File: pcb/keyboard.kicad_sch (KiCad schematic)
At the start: 60 parts, among them J1 Tag-Connect TC2030, J1 USB4510-03-1-A, J4 Battery, Q2 2N7002, SW1 PWR, U1 SRV05-4, U3 BQ24075, U3 BT840, Y1 32.768KHz

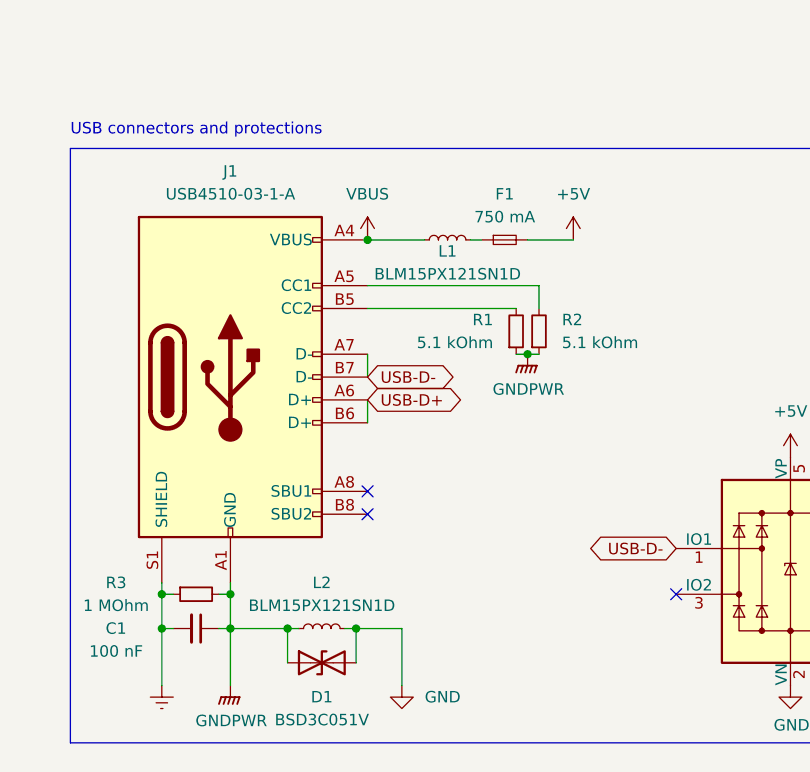
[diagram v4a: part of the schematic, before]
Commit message: #1 Change USB connector components to Digikey 0603
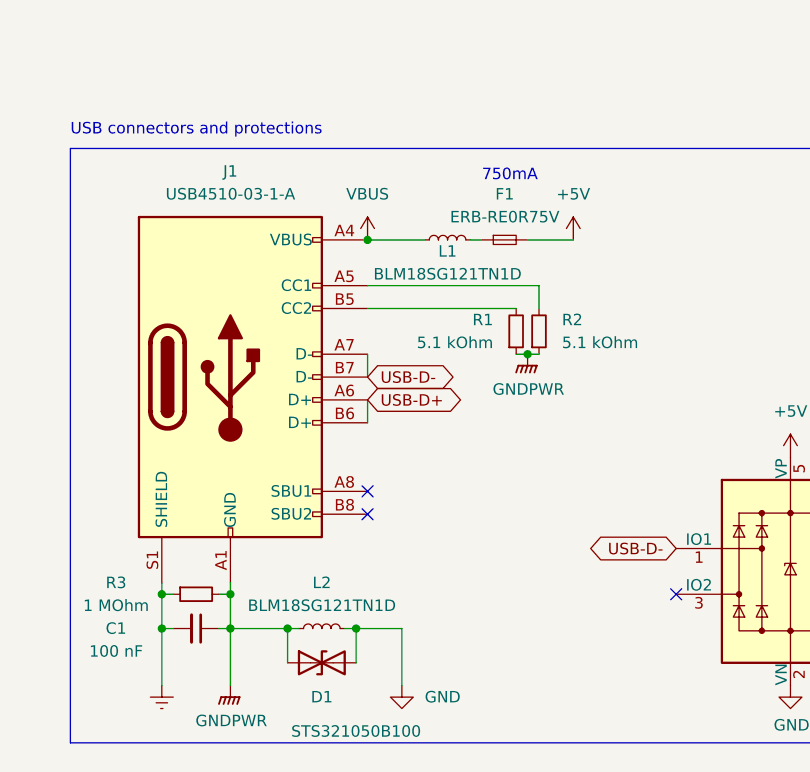
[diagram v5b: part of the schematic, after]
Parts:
- C1: footprint Capacitor_SMD:C_0402_1005Metric -> Capacitor_SMD:C_0603_1608Metric
- D1: value BSD3C051V -> STS321050B100
- F1: value 750 mA -> ERB-RE0R75V
- J1: footprint Connector_USB:USB_C_Receptacle_HRO_TYPE-C-31-M-12 -> keyboard:USB_C_Receptacle_GCT_USB4510-03-1-A
- L1, L2: value BLM15PX121SN1D -> BLM18SG121TN1D; footprint Inductor_SMD:L_0402_1005Metric -> Inductor_SMD:L_0603_1608Metric
- R1, R2, R3: footprint Resistor_SMD:R_0402_1005Metric -> Resistor_SMD:R_0603_1608Metric
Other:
- note added: "750mA"
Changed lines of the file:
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@@
     (effects (font (size 1.27 1.27)) (justify left bottom))
   )
+  (text "750mA" (at 67.31 213.36 0)
+    (effects (font (size 1.27 1.27)) (justify left bottom))
+  )
   (text "Battery management (advanced)" (at 242.57 26.67 0)
     (effects (font (size 1.27 1.27)) (justify left bottom))
@@
       (effects (font (size 1.27 1.27)) (justify right))
     )
-    (property "Footprint" "Resistor_SMD:R_0402_1005Metric" (at 71.12 229.87 0)
+    (property "Footprint" "Resistor_SMD:R_0603_1608Metric" (at 71.12 229.87 0)
       (effects (font (size 1.27 1.27)) hide)
     )
@@
       (effects (font (size 1.27 1.27)))
     )
-    (property "Value" "BLM15PX121SN1D" (at 63.5 223.52 90)
+    (property "Value" "BLM18SG121TN1D" (at 63.5 223.52 90)
       (effects (font (size 1.27 1.27)))
     )
-    (property "Footprint" "Inductor_SMD:L_0402_1005Metric" (at 63.5 219.71 0)
+    (property "Footprint" "Inductor_SMD:L_0603_1608Metric" (at 63.5 219.71 0)
       (effects (font (size 1.27 1.27)) hide)
     )
-    (property "Datasheet" "https://www.murata.com/en-us/products/productdata/8796740059166/ENFA0018.pdf" (at 63.5 219.71 0)
+    (property "Datasheet" "https://www.murata.com/en-us/products/productdata/8796738650142/ENFA0003.pdf" (at 63.5 219.71 0)
       (effects (font (size 1.27 1.27)) hide)
     )
@@
       (effects (font (size 1.27 1.27)))
     )
-    (property "Footprint" "Resistor_SMD:R_0402_1005Metric" (at 35.56 259.08 0)
+    (property "Footprint" "Resistor_SMD:R_0603_1608Metric" (at 35.56 259.08 0)
       (effects (font (size 1.27 1.27)) hide)
     )
@@
       (effects (font (size 1.27 1.27)))
     )
-    (property "Footprint" "Capacitor_SMD:C_0402_1005Metric" (at 35.56 262.89 0)
+    (property "Footprint" "Capacitor_SMD:C_0603_1608Metric" (at 35.56 262.89 0)
       (effects (font (size 1.27 1.27)) hide)
     )
@@
       (effects (font (size 1.27 1.27)))
     )
-    (property "Value" "BLM15PX121SN1D" (at 49.53 260.35 90)
+    (property "Value" "BLM18SG121TN1D" (at 49.53 260.35 90)
       (effects (font (size 1.27 1.27)))
     )
-    (property "Footprint" "Inductor_SMD:L_0402_1005Metric" (at 49.53 262.89 0)
+    (property "Footprint" "Inductor_SMD:L_0603_1608Metric" (at 49.53 262.89 0)
       (effects (font (size 1.27 1.27)) hide)
     )
-    (property "Datasheet" "~" (at 49.53 262.89 0)
+    (property "Datasheet" "https://www.murata.com/en-us/products/productdata/8796738650142/ENFA0003.pdf" (at 49.53 262.89 0)
       (effects (font (size 1.27 1.27)) hide)
     )
@@
   )
   (symbol (lib_id "Device:D_TVS") (at 49.53 266.7 0) (unit 1)
-    (in_bom yes) (on_board yes) (dnp no) (fields_autoplaced)
+    (in_bom yes) (on_board yes) (dnp no)
     (property "Reference" "D1" (at 49.53 270.51 0)
       (effects (font (size 1.27 1.27)))
     )
-    (property "Value" "BSD3C051V" (at 49.53 273.05 0)
+    (property "Value" "STS321050B100" (at 53.34 274.32 0)
       (effects (font (size 1.27 1.27)))
     )
@@
       (effects (font (size 1.27 1.27)) hide)
     )
-    (property "Datasheet" "~" (at 49.53 266.7 0)
+    (property "Datasheet" "https://www.eaton.com/content/dam/eaton/products/electronic-components/resources/data-sheet/eaton-sts321xxxbxx0-tvs-diode-esd-suppressor-data-sheet.pdf" (at 49.53 266.7 0)
       (effects (font (size 1.27 1.27)) hide)
     )
@@
       (effects (font (size 1.27 1.27)))
     )
-    (property "Value" "750 mA" (at 69.85 217.17 0)
+    (property "Value" "ERB-RE0R75V" (at 69.85 217.17 0)
       (effects (font (size 1.27 1.27)))
     )
@@
       (effects (font (size 1.27 1.27)) hide)
     )
-    (property "Datasheet" "~" (at 69.85 219.71 0)
+    (property "Datasheet" "https://industrial.panasonic.com/cdbs/www-data/pdf/AFA0000/AFA0000C7.pdf" (at 69.85 219.71 0)
       (effects (font (size 1.27 1.27)) hide)
     )
@@
       (effects (font (size 1.27 1.27)))
     )
-    (property "Footprint" "Connector_USB:USB_C_Receptacle_HRO_TYPE-C-31-M-12" (at 43.18 234.95 0)
+    (property "Footprint" "keyboard:USB_C_Receptacle_GCT_USB4510-03-1-A" (at 43.18 234.95 0)
       (effects (font (size 1.27 1.27)) hide)
     )
@@
       (effects (font (size 1.27 1.27)) (justify left))
     )
-    (property "Footprint" "Resistor_SMD:R_0402_1005Metric" (at 73.66 229.87 0)
+    (property "Footprint" "Resistor_SMD:R_0603_1608Metric" (at 73.66 229.87 0)
       (effects (font (size 1.27 1.27)) hide)
     )

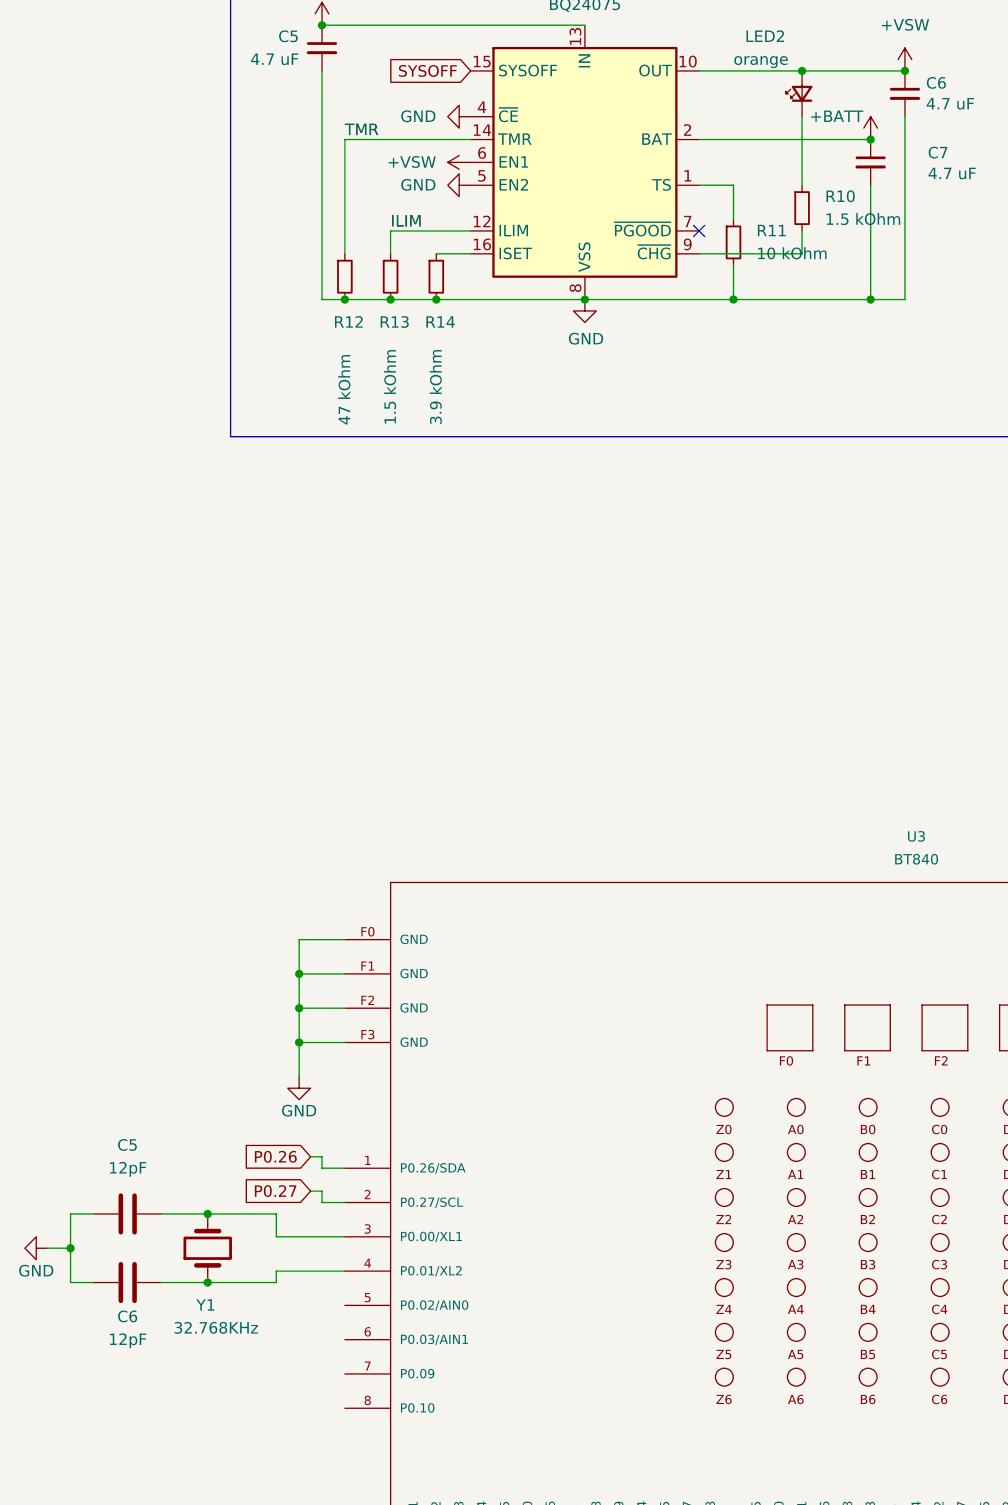
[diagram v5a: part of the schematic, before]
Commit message: #1 Choose/calculate 32khz crystal. Change all Caps and Res to 0603
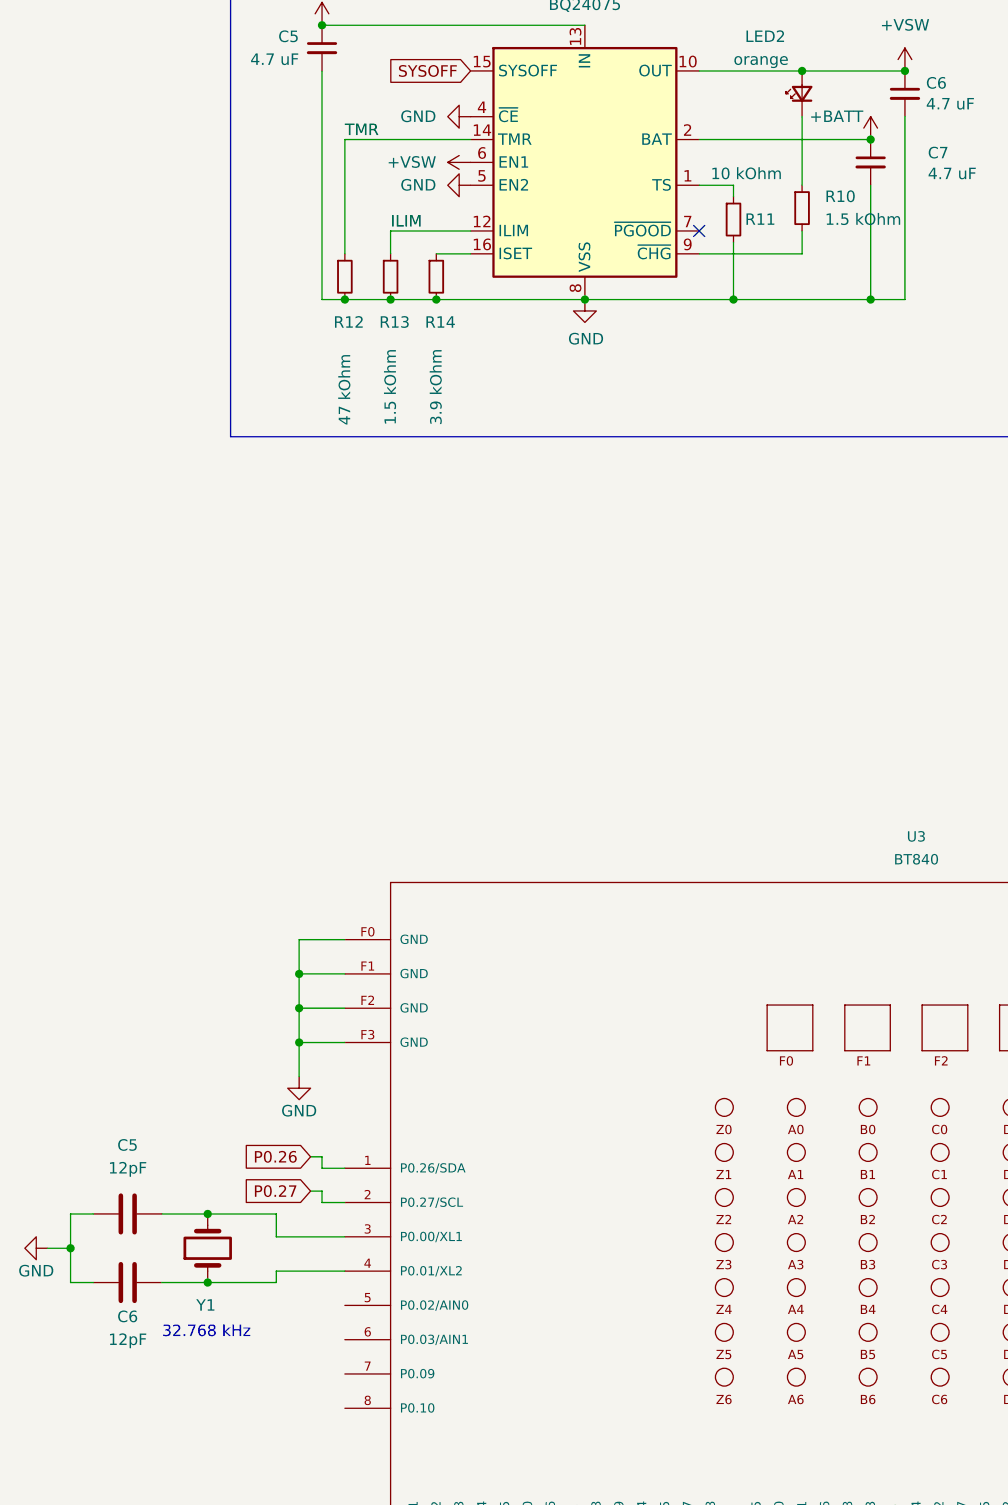
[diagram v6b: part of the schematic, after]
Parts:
- C5, C6, C7: footprint Capacitor_SMD:C_0402_1005Metric -> Capacitor_SMD:C_0603_1608Metric
- C5, C6: footprint (none) -> Capacitor_SMD:C_0603_1608Metric
- LED2: footprint LED_SMD:LED_0402_1005Metric -> LED_SMD:LED_0603_1608Metric
- R10, R11, R13, R14, R4, R5, R8: footprint Resistor_SMD:R_0402_1005Metric -> Resistor_SMD:R_0603_1608Metric
- U3: footprint BT840_BT840 -> keyboard:Fanstel_BT840
- Y1: value 32.768KHz -> ECS-.327-9-34B-TR; footprint (none) -> Crystal:Crystal_SMD_3215-2Pin_3.2x1.5mm; Digikey (none) -> https://www.digikey.fr/short/w4d4tdrt; Notes (none) -> 32.768 kHz ±20ppm Crystal 9pF 70 kOhms 2-SMD, No Lead
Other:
- note added: "32.768 kHz"
- moved on the sheet: R11
